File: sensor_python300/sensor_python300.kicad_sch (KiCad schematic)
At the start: 71 parts, among them J101 DF40HC(4.0)-60DS-0.4V(51), U101 NOIP1SN0300A-QTI, U102 TPS7A2033PDBVR, U103 TPS22918DBVR, U104 TPS7A2033PDBVR, U105 APX803S, U106 TPS610995DRVR, X101 <DNP> DSC1103DI5-360.0000

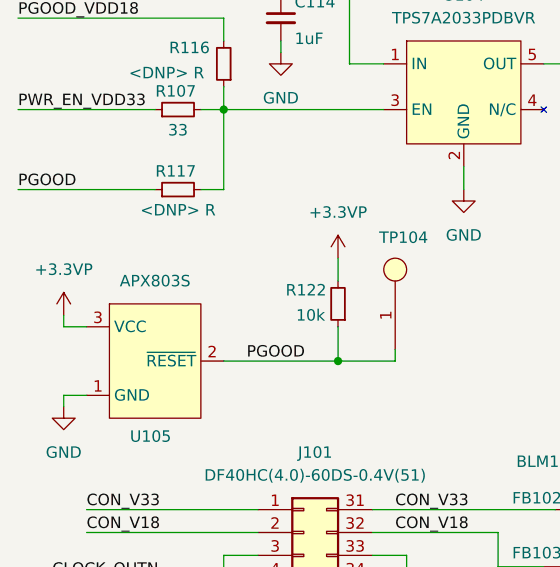
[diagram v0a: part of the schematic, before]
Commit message: Update KiCad project files for sensor_python300 and mipi_spartan7: adjust active layer, visibility settings, and add default application options
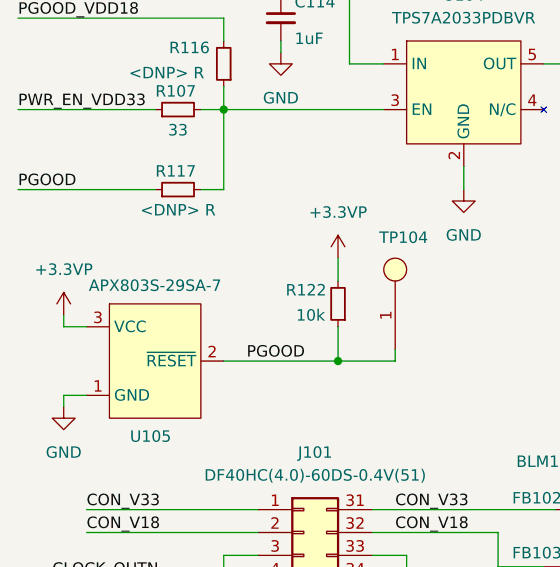
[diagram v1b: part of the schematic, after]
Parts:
- U105: value APX803S -> APX803S-29SA-7
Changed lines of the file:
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@@
 			)
 		)
-		(property "Value" "APX803S"
-			(at 29.21 88.9 0)
+		(property "Value" "APX803S-29SA-7"
+			(at 29.21 89.408 0)
 			(effects
 				(font

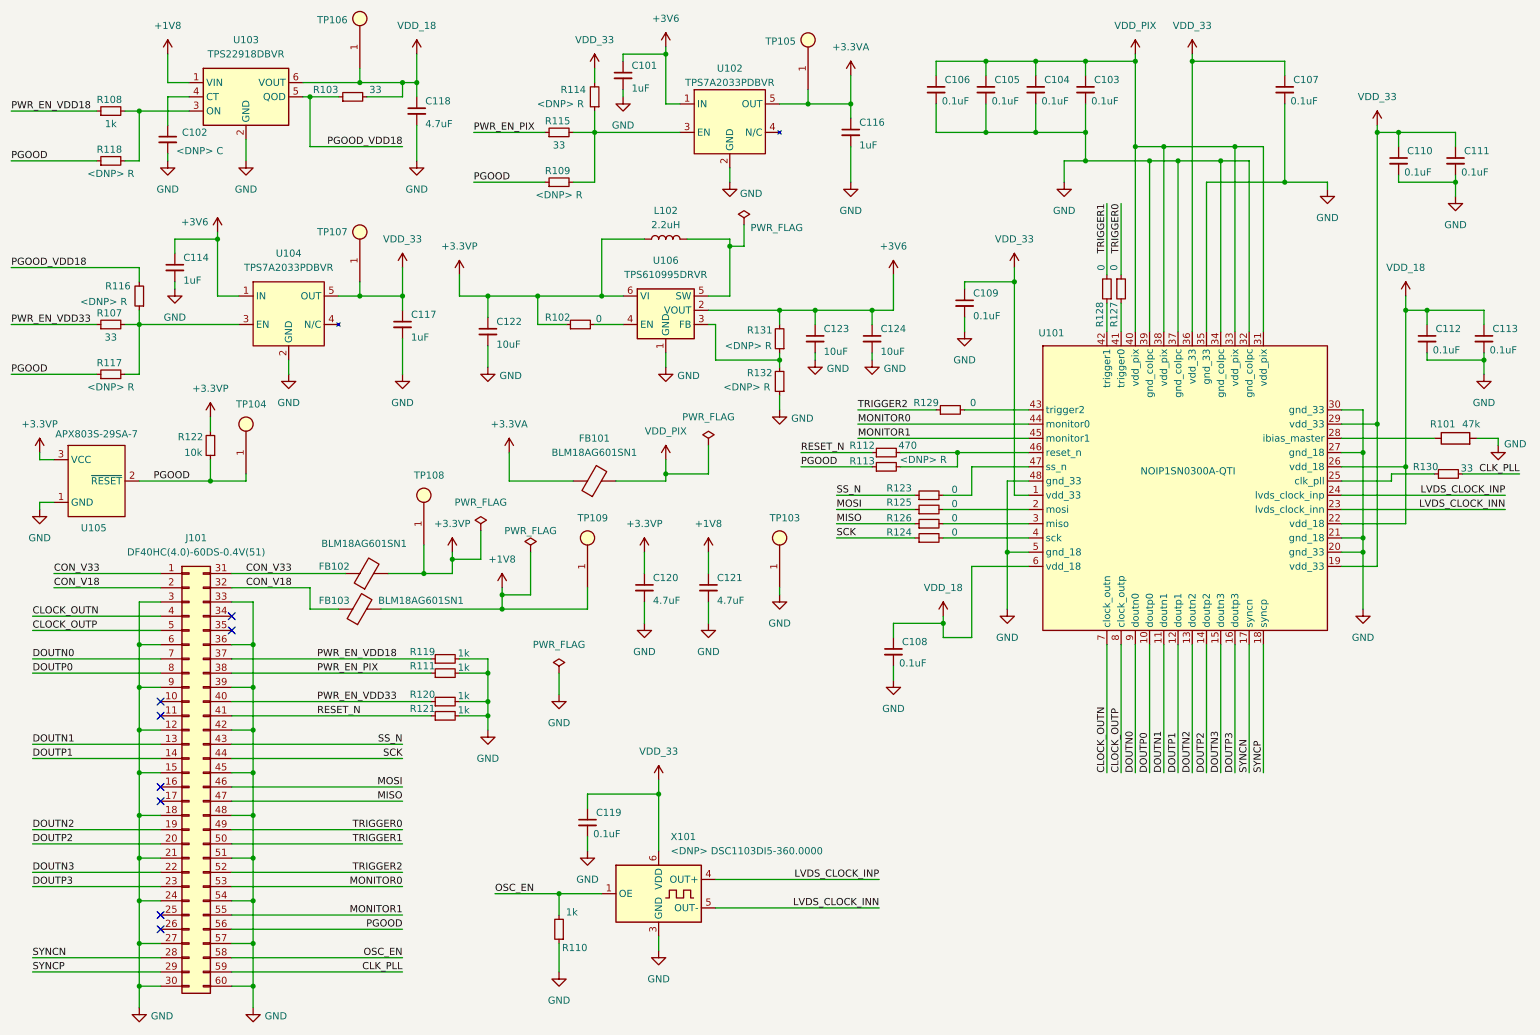
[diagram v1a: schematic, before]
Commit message: コンデンサ追加
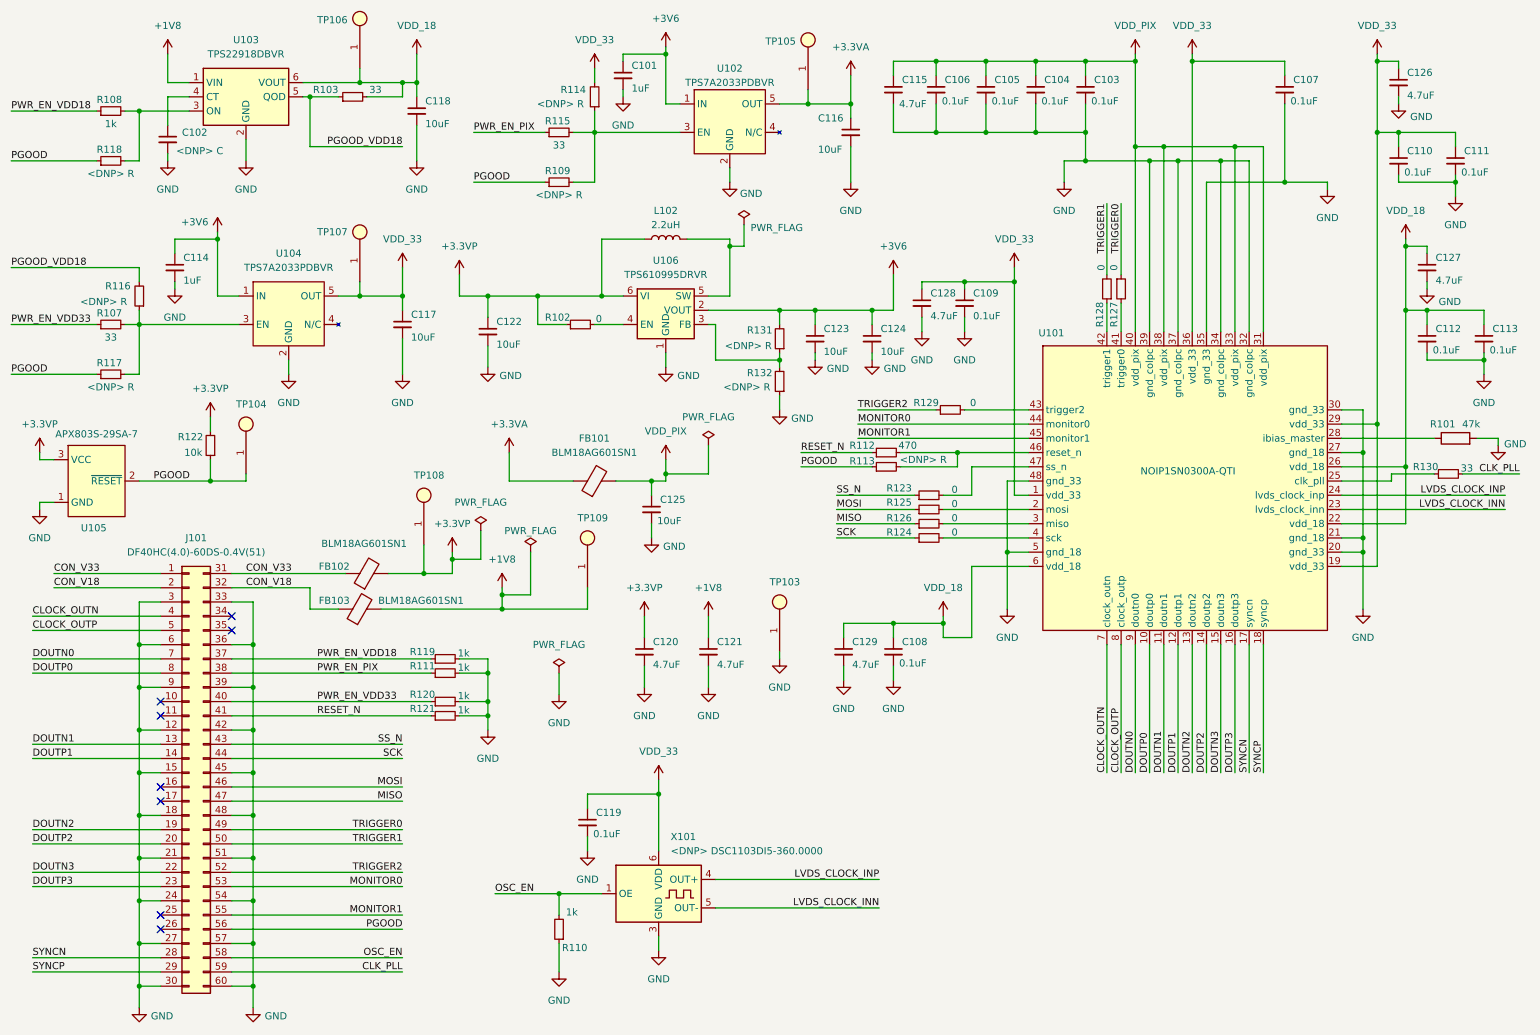
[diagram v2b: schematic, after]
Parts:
- added C115, C126, C127, C128, C129: 4.7uF, Capacitor_SMD:C_0402_1005Metric, symbol Device:C_Small
- added C125: 10uF, Capacitor_SMD:C_0402_1005Metric, symbol Device:C_Small
- C116, C117: value 1uF -> 10uF
- C118: value 4.7uF -> 10uF
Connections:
- net GND: now also C115.2, C125.2, C126.2, C127.2, C128.2, C129.2
- net VDD_18: now also C127.1, C129.1
- net VDD_33: now also C126.1, C128.1
- net VDD_PIX: now also C115.1, C125.1
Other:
- moved on the sheet: C120, C121, TP103

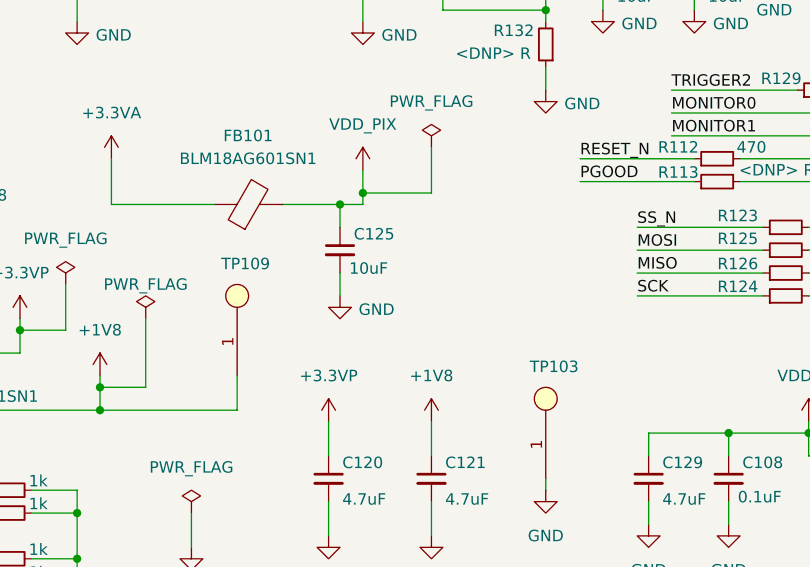
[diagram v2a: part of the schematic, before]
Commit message: Update schematic and project settings for sensor_python300
- Modified selection filter in project settings to enable footprint and text visibility.
- Updated visible layers configuration for better layer management.
- Added new junctions and wires in the schematic to improve connectivity.
- Introduced a new capacitor (C130) with appropriate properties and connections.
- Replaced the existing GND symbol with a new instance for better clarity and organization.
- Adjusted positions of several components for improved layout and readability.
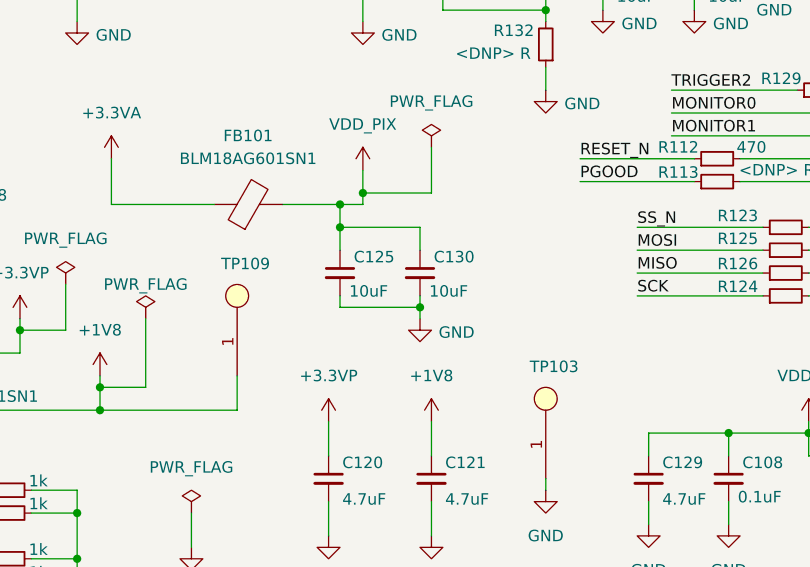
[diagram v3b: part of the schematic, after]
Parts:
- added C130: 10uF, Capacitor_SMD:C_0603_1608Metric, symbol Device:C_Small
- C125: footprint Capacitor_SMD:C_0402_1005Metric -> Capacitor_SMD:C_0603_1608Metric
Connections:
- net GND: now also C130.2
- net VDD_PIX: now also C130.1
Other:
- moved on the sheet: C125
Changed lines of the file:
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@@
 	)
 	(junction
+		(at 128.27 100.33)
+		(diameter 0)
+		(color 0 0 0 0)
+	)
+	(junction
 		(at 119.38 64.77)
 		(diameter 0)
@@
 	)
 	(junction
+		(at 137.16 109.22)
+		(diameter 0)
+		(color 0 0 0 0)
+	)
+	(junction
 		(at 241.3 44.45)
 		(diameter 0)
@@
 	(wire
 		(pts
+			(xy 137.16 100.33) (xy 137.16 102.87)
+		)
+		(stroke
+			(width 0)
+			(type default)
+		)
+	)
+	(wire
+		(pts
 			(xy 138.43 67.31) (xy 151.13 67.31)
 		)
@@
 	(wire
 		(pts
+			(xy 128.27 100.33) (xy 128.27 102.87)
+		)
+		(stroke
+			(width 0)
+			(type default)
+		)
+	)
+	(wire
+		(pts
 			(xy 111.76 171.45) (xy 111.76 175.26)
 		)
@@
 	(wire
 		(pts
+			(xy 128.27 109.22) (xy 137.16 109.22)
+		)
+		(stroke
+			(width 0)
+			(type default)
+		)
+	)
+	(wire
+		(pts
 			(xy 255.27 107.95) (xy 255.27 110.49)
 		)
@@
 	(wire
 		(pts
+			(xy 137.16 109.22) (xy 137.16 110.49)
+		)
+		(stroke
+			(width 0)
+			(type default)
+		)
+	)
+	(wire
+		(pts
 			(xy 40.64 132.08) (xy 17.78 132.08)
 		)
@@
 	(wire
 		(pts
+			(xy 137.16 107.95) (xy 137.16 109.22)
+		)
+		(stroke
+			(width 0)
+			(type default)
+		)
+	)
+	(wire
+		(pts
 			(xy 196.85 22.86) (xy 196.85 25.4)
 		)
@@
 	(wire
 		(pts
+			(xy 128.27 100.33) (xy 137.16 100.33)
+		)
+		(stroke
+			(width 0)
+			(type default)
+		)
+	)
+	(wire
+		(pts
 			(xy 34.29 31.75) (xy 36.83 31.75)
 		)
@@
 	(wire
 		(pts
-			(xy 128.27 105.41) (xy 128.27 107.95)
+			(xy 128.27 107.95) (xy 128.27 109.22)
 		)
 		(stroke
@@
 		)
 		(instances
-			(project ""
+			(project "sensor_python300"
 				(path "/c2c18cad-31cc-478f-ac04-d4c87cc32d8d"
 					(reference "#FLG01")
@@
 		)
 		(instances
-			(project ""
+			(project "sensor_python300"
 				(path "/c2c18cad-31cc-478f-ac04-d4c87cc32d8d"
 					(reference "#PWR037")
@@
 		)
 		(instances
-			(project ""
+			(project "sensor_python300"
 				(path "/c2c18cad-31cc-478f-ac04-d4c87cc32d8d"
 					(reference "U102")
@@
 		)
 		(instances
-			(project ""
+			(project "sensor_python300"
 				(path "/c2c18cad-31cc-478f-ac04-d4c87cc32d8d"
 					(reference "U101")
@@
 		)
 		(instances
-			(project ""
+			(project "sensor_python300"
 				(path "/c2c18cad-31cc-478f-ac04-d4c87cc32d8d"
 					(reference "FB101")
@@
 	(symbol
 		(lib_id "Device:C_Small")
+		(at 137.16 105.41 0)
+		(unit 1)
+		(exclude_from_sim no)
+		(in_bom yes)
+		(on_board yes)
+		(dnp no)
+		(property "Reference" "C130"
+			(at 138.684 103.632 0)
+			(effects
+				(font
+					(size 1.27 1.27)
+				)
+				(justify left)
+			)
+		)
+		(property "Value" "10uF"
+			(at 138.176 107.442 0)
+			(effects
+				(font
+					(size 1.27 1.27)
+				)
+				(justify left)
+			)
+		)
+		(property "Footprint" "Capacitor_SMD:C_0603_1608Metric"
+			(at 137.16 105.41 0)
+			(effects
+				(font
+					(size 1.27 1.27)
+				)
+				(hide yes)
+			)
+		)
+		(property "Datasheet" "~"
+			(at 137.16 105.41 0)
+			(effects
+				(font
+					(size 1.27 1.27)
+				)
+				(hide yes)
+			)
+		)
+		(property "Description" "Unpolarized capacitor, small symbol"
+			(at 137.16 105.41 0)
+			(effects
+				(font
+					(size 1.27 1.27)
+				)
+				(hide yes)
+			)
+		)
+		(pin "2"
+		)
+		(pin "1"
+		)
+		(instances
+			(project "sensor_python300"
+				(path "/c2c18cad-31cc-478f-ac04-d4c87cc32d8d"
+					(reference "C130")
+					(unit 1)
+				)
+			)
+		)
+	)
+	(symbol
+		(lib_id "Device:C_Small")
 		(at 163.83 35.56 0)
 		(unit 1)
@@
 	)
 	(symbol
-		(lib_id "power:GND")
-		(at 128.27 107.95 0)
-		(unit 1)
-		(exclude_from_sim no)
-		(in_bom yes)
-		(on_board yes)
-		(dnp no)
-		(property "Reference" "#PWR0113"
-			(at 128.27 114.3 0)
-			(effects
-				(font
-					(size 1.27 1.27)
-				)
-				(hide yes)
-			)
-		)
-		(property "Value" "GND"
-			(at 132.334 109.474 0)
-			(effects
-				(font
-					(size 1.27 1.27)
-				)
-			)
-		)
-		(property "Footprint" ""
-			(at 128.27 107.95 0)
-			(effects
-				(font
-					(size 1.27 1.27)
-				)
-				(hide yes)
-			)
-		)
-		(property "Datasheet" ""
-			(at 128.27 107.95 0)
-			(effects
-				(font
-					(size 1.27 1.27)
-				)
-				(hide yes)
-			)
-		)
-		(property "Description" "Power symbol creates a global label with name \"GND\" , ground"
-			(at 128.27 107.95 0)
-			(effects
-				(font
-					(size 1.27 1.27)
-				)
-				(hide yes)
-			)
-		)
-		(pin "1"
-		)
-		(instances
-			(project "sensor_python300"
-				(path "/c2c18cad-31cc-478f-ac04-d4c87cc32d8d"
-					(reference "#PWR0113")
-					(unit 1)
-				)
-			)
-		)
-	)
-	(symbol
 		(lib_id "power:+1V8")
 		(at 101.6 116.84 0)
@@
 		)
 		(instances
-			(project ""
+			(project "sensor_python300"
 				(path "/c2c18cad-31cc-478f-ac04-d4c87cc32d8d"
 					(reference "#PWR01")
@@
 		)
 		(instances
-			(project ""
+			(project "sensor_python300"
 				(path "/c2c18cad-31cc-478f-ac04-d4c87cc32d8d"
 					(reference "X101")
@@
 		)
 		(instances
-			(project ""
+			(project "sensor_python300"
 				(path "/c2c18cad-31cc-478f-ac04-d4c87cc32d8d"
 					(reference "#PWR0104")
@@
 		)
 		(instances
-			(project ""
+			(project "sensor_python300"
 				(path "/c2c18cad-31cc-478f-ac04-d4c87cc32d8d"
 					(reference "L102")
@@
 		)
 		(instances
-			(project ""
+			(project "sensor_python300"
 				(path "/c2c18cad-31cc-478f-ac04-d4c87cc32d8d"
 					(reference "R101")
@@
 		)
 		(instances
-			(project ""
+			(project "sensor_python300"
 				(path "/c2c18cad-31cc-478f-ac04-d4c87cc32d8d"
 					(reference "#PWR014")
@@
 	)
 	(symbol
+		(lib_id "power:GND")
+		(at 137.16 110.49 0)
+		(unit 1)
+		(exclude_from_sim no)
+		(in_bom yes)
+		(on_board yes)
+		(dnp no)
+		(property "Reference" "#PWR0118"
+			(at 137.16 116.84 0)
+			(effects
+				(font
+					(size 1.27 1.27)
+				)
+				(hide yes)
+			)
+		)
+		(property "Value" "GND"
+			(at 141.224 112.014 0)
+			(effects
+				(font
+					(size 1.27 1.27)
+				)
+			)
+		)
+		(property "Footprint" ""
+			(at 137.16 110.49 0)
+			(effects
+				(font
+					(size 1.27 1.27)
+				)
+				(hide yes)
+			)
+		)
+		(property "Datasheet" ""
+			(at 137.16 110.49 0)
+			(effects
+				(font
+					(size 1.27 1.27)
+				)
+				(hide yes)
+			)
+		)
+		(property "Description" "Power symbol creates a global label with name \"GND\" , ground"
+			(at 137.16 110.49 0)
+			(effects
+				(font
+					(size 1.27 1.27)
+				)
+				(hide yes)
+			)
+		)
+		(pin "1"
+		)
+		(instances
+			(project "sensor_python300"
+				(path "/c2c18cad-31cc-478f-ac04-d4c87cc32d8d"
+					(reference "#PWR0118")
+					(unit 1)
+				)
+			)
+		)
+	)
+	(symbol
 		(lib_id "power:+3.3VP")
 		(at 19.05 92.71 0)
@@
 		)
 		(instances
-			(project ""
+			(project "sensor_python300"
 				(path "/c2c18cad-31cc-478f-ac04-d4c87cc32d8d"
 					(reference "U105")
@@
 	(symbol
 		(lib_id "Device:C_Small")
-		(at 128.27 102.87 0)
+		(at 128.27 105.41 0)
 		(unit 1)
 		(exclude_from_sim no)
@@
 		(dnp no)
 		(property "Reference" "C125"
-			(at 129.794 101.092 0)
+			(at 129.794 103.632 0)
 			(effects
 				(font
@@
 		)
 		(property "Value" "10uF"
-			(at 129.286 104.902 0)
+			(at 129.286 107.442 0)
 			(effects
 				(font
@@
 			)
 		)
-		(property "Footprint" "Capacitor_SMD:C_0402_1005Metric"
-			(at 128.27 102.87 0)
+		(property "Footprint" "Capacitor_SMD:C_0603_1608Metric"
+			(at 128.27 105.41 0)
 			(effects
 				(font
@@
 		)
 		(property "Datasheet" "~"
-			(at 128.27 102.87 0)
+			(at 128.27 105.41 0)
 			(effects
 				(font
@@
 		)
 		(property "Description" "Unpolarized capacitor, small symbol"
-			(at 128.27 102.87 0)
+			(at 128.27 105.41 0)
 			(effects
 				(font
